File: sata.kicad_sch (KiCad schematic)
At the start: 18 parts, among them J4 SATA_Backplane, U1 NCP45521, U2 NCP45521

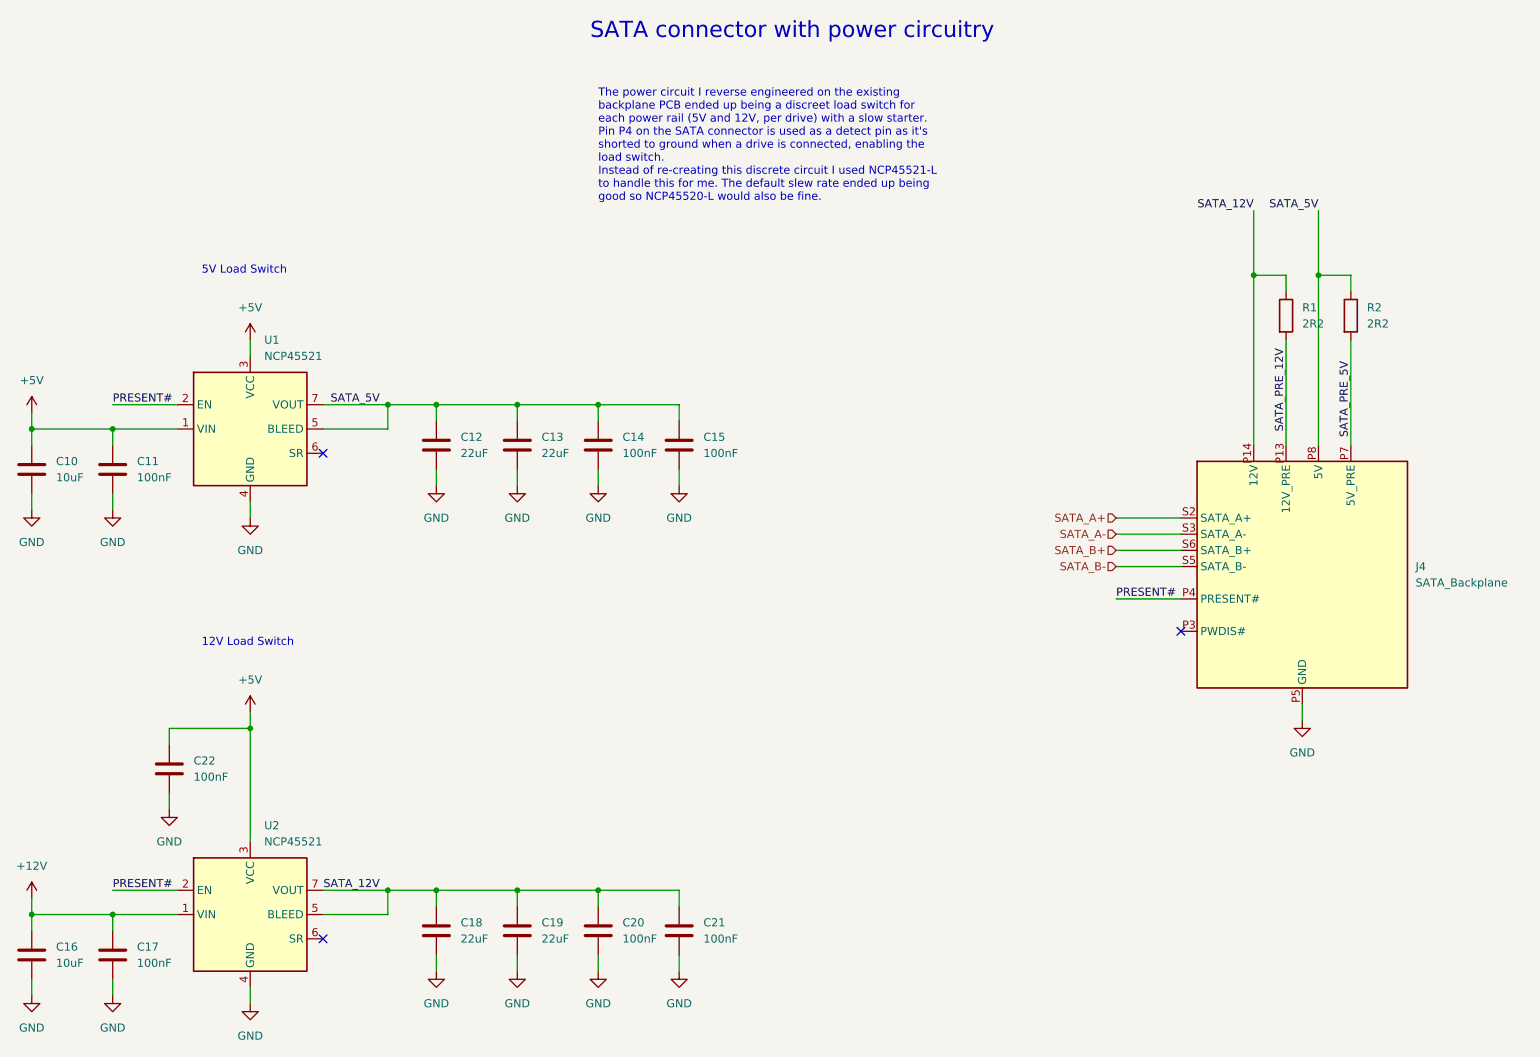
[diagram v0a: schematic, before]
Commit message: no DRC errors
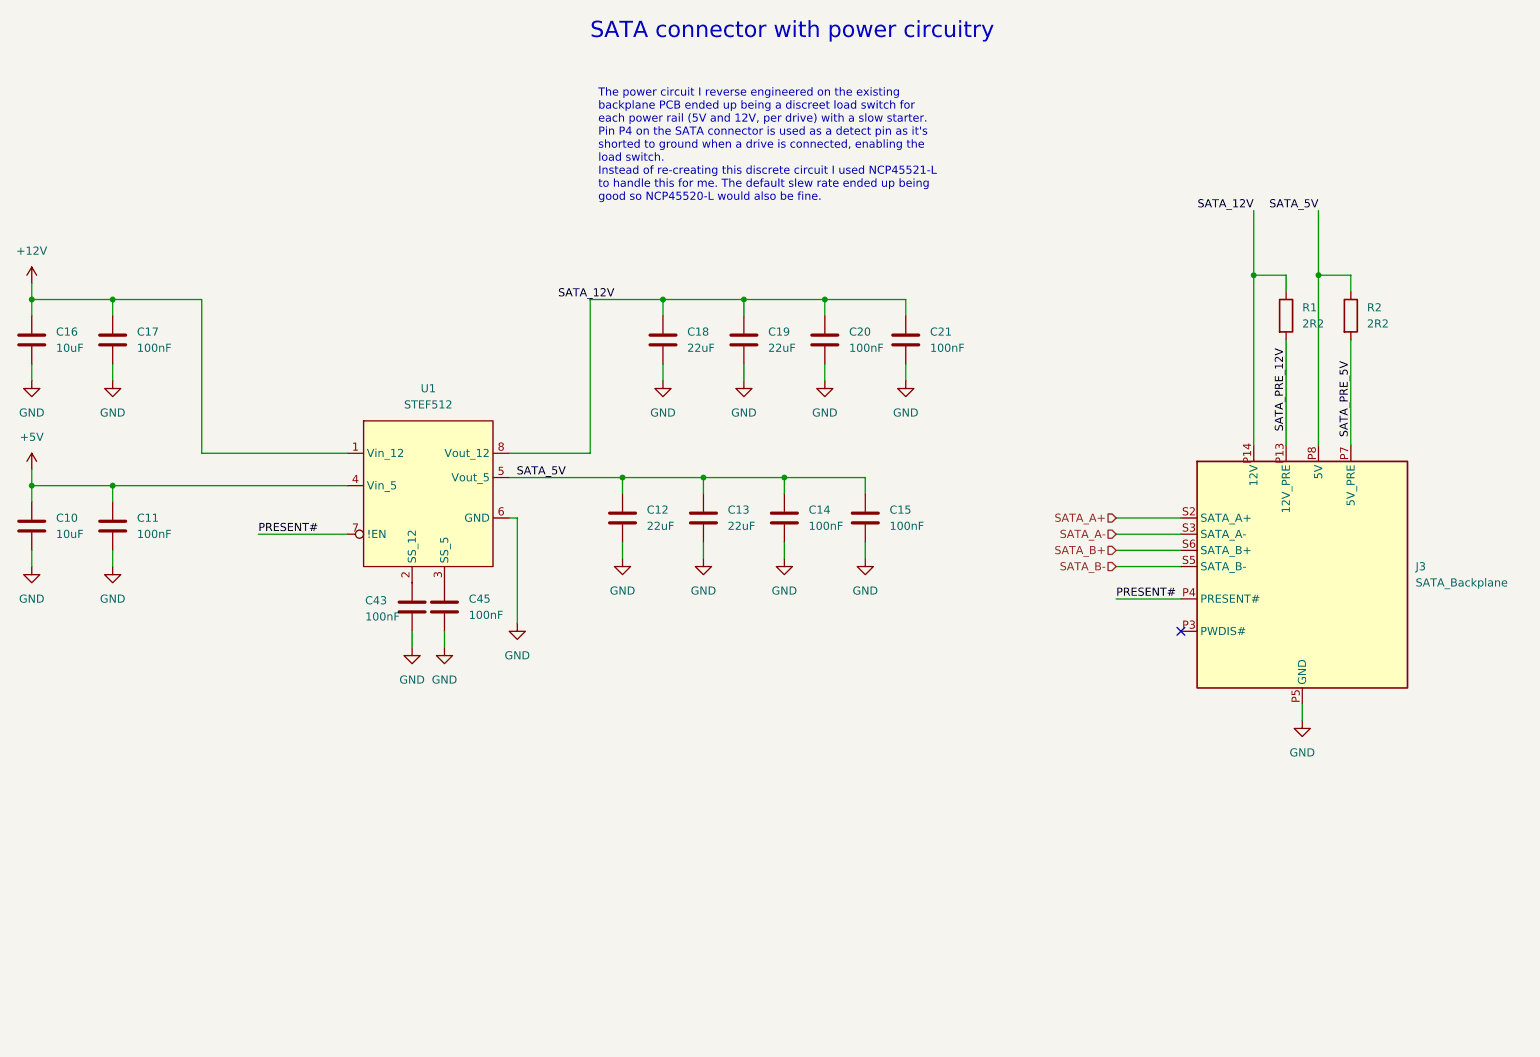
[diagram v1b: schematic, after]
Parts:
- removed C22: 100nF, Capacitor_SMD:C_0603_1608Metric, symbol Device:C
- removed U1, U2: NCP45521, Load_Switches:NCP45521, symbol Load_Switches:NCP45521
- added C43, C45: 100nF, Capacitor_SMD:C_0603_1608Metric, symbol Device:C
- added U1: STEF512, TSOT23-8L, symbol Load_Switches:STEF512
- renumbered J4 to J3
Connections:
- net +12V: now also U1.1 (Vin_12)
- net +5V: now also U1.4 (Vin_5)
- net GND: now also C43.2, C45.2, U1.6 (GND)
- net PRESENT#: now also U1.7 (!EN)
- net SATA_12V: now also U1.8 (Vout_12)
- net SATA_5V: now also U1.5 (Vout_5)
- new net: C45.1, U1.3 (SS_5)
- new net: C43.1, U1.2 (SS_12)
- no-connect marks 3 -> 1
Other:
- note removed: "12V Load Switch"
- note removed: "5V Load Switch"
- moved on the sheet: C10, C11, C12, C13, C14, C15, C16, C17, C18, C19, C20, C21
